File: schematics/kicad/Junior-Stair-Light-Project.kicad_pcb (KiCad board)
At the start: 2 copper layers, 64 x 80 mm, 72 parts, among them J1 12V Eingang, J2 LED_stripes_per_step, T1_1 BC337, T1_10 BC327, T1_11 BC337, T1_12 BC337, T1_13 BC337, T1_14 BC337, T1_15 BC337, T1_16 BC327, T1_17 BC327, T1_18 BC327, T1_19 BC327, T1_2 BC327, T1_20 BC327, T1_21 BC337, T1_22 BC337, T1_23 BC337, T1_24 BC327, T1_25 BC327, T1_26 BC327, T1_3 BC337, T1_4 BC337, T1_5 BC337, T1_6 BC337, T1_7 BC327, T1_8 BC327, T1_9 BC327, U1 L4940V5, U2 Arduino_Nano

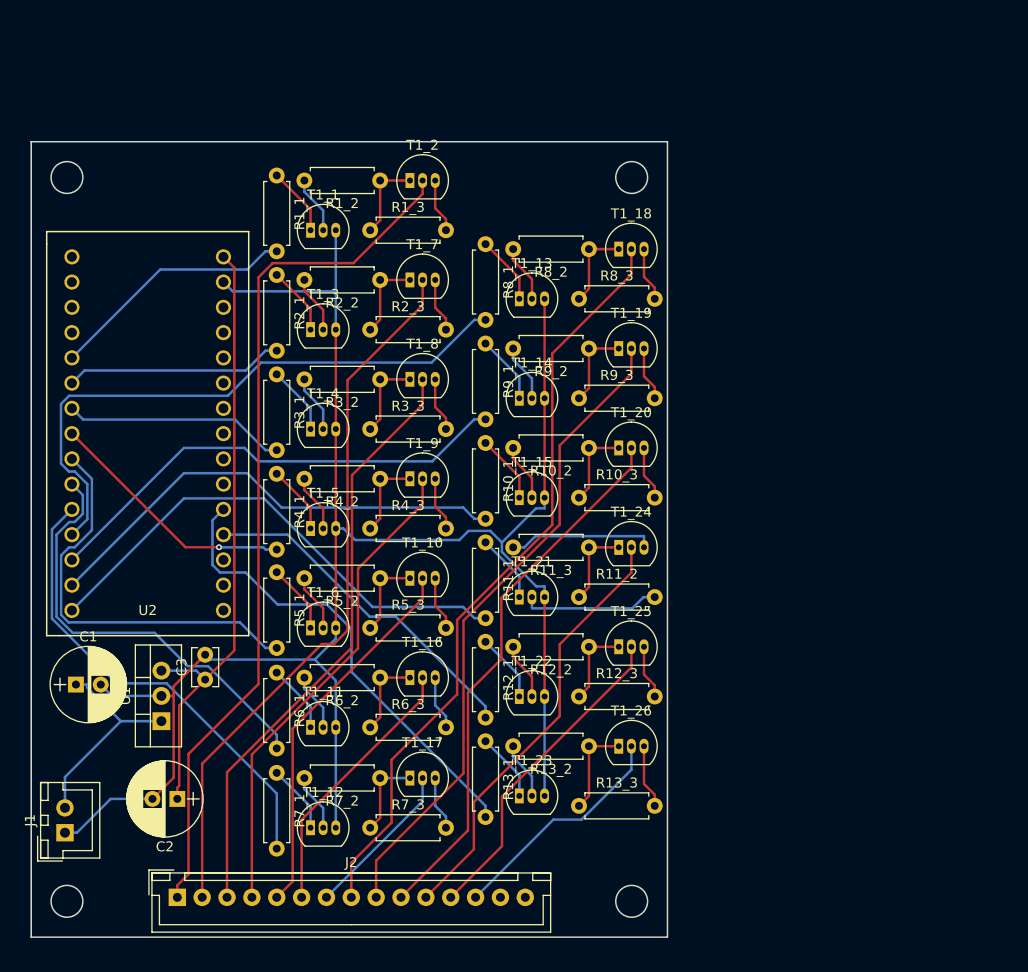
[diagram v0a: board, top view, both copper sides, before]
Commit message: Added max channels (19) and finished first RC of PCB layout
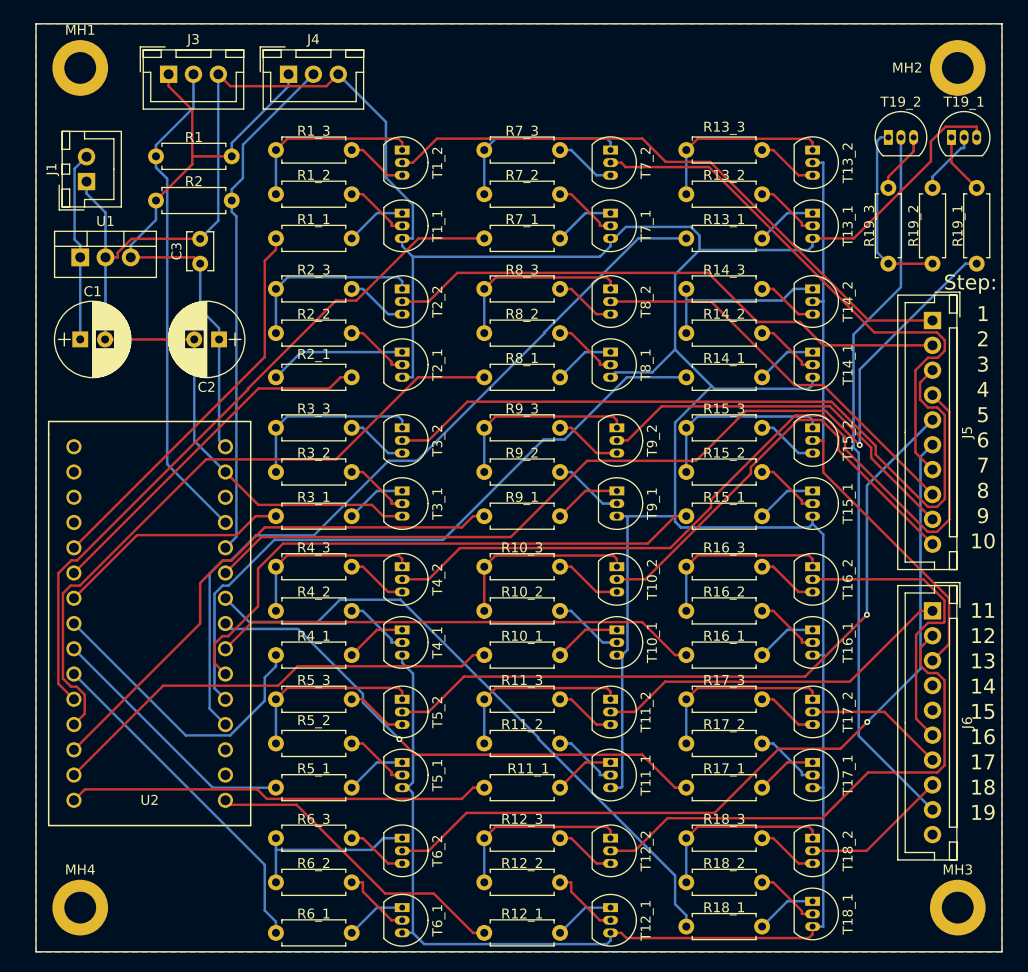
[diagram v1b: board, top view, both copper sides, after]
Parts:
- removed J2: LED_stripes_per_step, Connectors_JST:JST_XH_B15B-XH-A_15x2.50mm_Straight
- removed T1_10, T1_16, T1_17, T1_18, T1_19, T1_20, T1_24, T1_25, T1_26, T1_7, T1_8, T1_9: BC327, TO_SOT_Packages_THT:TO-92_Inline_Narrow_Oval
- removed T1_11, T1_12, T1_13, T1_14, T1_15, T1_21, T1_22, T1_23, T1_3, T1_4, T1_5, T1_6: BC337, TO_SOT_Packages_THT:TO-92_Inline_Narrow_Oval
- added J3: CONN_01X03, Connectors_JST:JST_XH_B03B-XH-A_03x2.50mm_Straight, F.Cu at (123.8, 69.2)
- added J4: CONN_01X03, Connectors_JST:JST_XH_B03B-XH-A_03x2.50mm_Straight, F.Cu at (135.9, 69.2)
- added J5: Conn_01x10, Connectors_JST:JST_XH_B10B-XH-A_10x2.50mm_Straight, F.Cu at (200.7, 94.0)
- added J6: Conn_01x10, Connectors_JST:JST_XH_B10B-XH-A_10x2.50mm_Straight, F.Cu at (200.7, 123.2)
- added MH1: MH1, Mounting_Holes:MountingHole_3.2mm_M3_DIN965_Pad, F.Cu at (114.9, 68.6)
- added MH2: MH2, Mounting_Holes:MountingHole_3.2mm_M3_DIN965_Pad, F.Cu at (203.2, 68.6)
- added MH3: MH3, Mounting_Holes:MountingHole_3.2mm_M3_DIN965_Pad, F.Cu at (203.2, 153.0)
- added MH4: MH4, Mounting_Holes:MountingHole_3.2mm_M3_DIN965_Pad, F.Cu at (114.9, 153.0)
- added R1: 10k, Resistors_THT:R_Axial_DIN0207_L6.3mm_D2.5mm_P7.62mm_Horizontal, F.Cu at (130.2, 77.5)
- added R14_1: 10k, Resistors_THT:R_Axial_DIN0207_L6.3mm_D2.5mm_P7.62mm_Horizontal, F.Cu at (183.5, 99.7)
- added R14_2: 1k, Resistors_THT:R_Axial_DIN0207_L6.3mm_D2.5mm_P7.62mm_Horizontal, F.Cu at (175.9, 95.2)
- added R14_3: 1k, Resistors_THT:R_Axial_DIN0207_L6.3mm_D2.5mm_P7.62mm_Horizontal, F.Cu at (175.9, 90.8)
- added R15_1: 10k, Resistors_THT:R_Axial_DIN0207_L6.3mm_D2.5mm_P7.62mm_Horizontal, F.Cu at (183.5, 113.7)
- added R15_2: 1k, Resistors_THT:R_Axial_DIN0207_L6.3mm_D2.5mm_P7.62mm_Horizontal, F.Cu at (175.9, 109.2)
- added R15_3: 1k, Resistors_THT:R_Axial_DIN0207_L6.3mm_D2.5mm_P7.62mm_Horizontal, F.Cu at (175.9, 104.8)
- added R16_1: 10k, Resistors_THT:R_Axial_DIN0207_L6.3mm_D2.5mm_P7.62mm_Horizontal, F.Cu at (183.5, 127.6)
- added R16_2: 1k, Resistors_THT:R_Axial_DIN0207_L6.3mm_D2.5mm_P7.62mm_Horizontal, F.Cu at (175.9, 123.2)
- added R16_3: 1k, Resistors_THT:R_Axial_DIN0207_L6.3mm_D2.5mm_P7.62mm_Horizontal, F.Cu at (175.9, 118.7)
- added R17_1: 10k, Resistors_THT:R_Axial_DIN0207_L6.3mm_D2.5mm_P7.62mm_Horizontal, F.Cu at (183.5, 141.0)
- added R17_2: 1k, Resistors_THT:R_Axial_DIN0207_L6.3mm_D2.5mm_P7.62mm_Horizontal, F.Cu at (175.9, 136.5)
- added R17_3: 1k, Resistors_THT:R_Axial_DIN0207_L6.3mm_D2.5mm_P7.62mm_Horizontal, F.Cu at (175.9, 132.1)
- added R18_1: 10k, Resistors_THT:R_Axial_DIN0207_L6.3mm_D2.5mm_P7.62mm_Horizontal, F.Cu at (183.5, 154.9)
- added R18_2: 1k, Resistors_THT:R_Axial_DIN0207_L6.3mm_D2.5mm_P7.62mm_Horizontal, F.Cu at (175.9, 150.5)
- added R18_3: 1k, Resistors_THT:R_Axial_DIN0207_L6.3mm_D2.5mm_P7.62mm_Horizontal, F.Cu at (175.9, 146.1)
- added R19_1: 10k, Resistors_THT:R_Axial_DIN0207_L6.3mm_D2.5mm_P7.62mm_Horizontal, F.Cu at (205.1, 80.6)
- added R19_2: 1k, Resistors_THT:R_Axial_DIN0207_L6.3mm_D2.5mm_P7.62mm_Horizontal, F.Cu at (200.7, 88.3)
- added R19_3: 1k, Resistors_THT:R_Axial_DIN0207_L6.3mm_D2.5mm_P7.62mm_Horizontal, F.Cu at (196.2, 88.3)
- added R2: 10k, Resistors_THT:R_Axial_DIN0207_L6.3mm_D2.5mm_P7.62mm_Horizontal, F.Cu at (122.6, 81.9)
- added T10_1: BC337, TO_SOT_Packages_THT:TO-92_Inline_Narrow_Oval, F.Cu at (168.9, 125.1)
- added T10_2: BC327, TO_SOT_Packages_THT:TO-92_Inline_Narrow_Oval, F.Cu at (168.9, 118.7)
- added T11_1: BC337, TO_SOT_Packages_THT:TO-92_Inline_Narrow_Oval, F.Cu at (168.3, 138.4)
- added T11_2: BC327, TO_SOT_Packages_THT:TO-92_Inline_Narrow_Oval, F.Cu at (168.3, 132.1)
- added T12_1: BC337, TO_SOT_Packages_THT:TO-92_Inline_Narrow_Oval, F.Cu at (168.3, 153.0)
- added T12_2: BC327, TO_SOT_Packages_THT:TO-92_Inline_Narrow_Oval, F.Cu at (168.3, 146.1)
- added T13_1: BC337, TO_SOT_Packages_THT:TO-92_Inline_Narrow_Oval, F.Cu at (188.6, 83.2)
- added T13_2: BC327, TO_SOT_Packages_THT:TO-92_Inline_Narrow_Oval, F.Cu at (188.6, 76.8)
- added T14_1: BC337, TO_SOT_Packages_THT:TO-92_Inline_Narrow_Oval, F.Cu at (188.6, 97.2)
- added T14_2: BC327, TO_SOT_Packages_THT:TO-92_Inline_Narrow_Oval, F.Cu at (188.6, 90.8)
- added T15_1: BC337, TO_SOT_Packages_THT:TO-92_Inline_Narrow_Oval, F.Cu at (188.6, 111.1)
- added T15_2: BC327, TO_SOT_Packages_THT:TO-92_Inline_Narrow_Oval, F.Cu at (188.6, 104.8)
- added T16_1: BC337, TO_SOT_Packages_THT:TO-92_Inline_Narrow_Oval, F.Cu at (188.6, 125.1)
- added T16_2: BC327, TO_SOT_Packages_THT:TO-92_Inline_Narrow_Oval, F.Cu at (188.6, 118.7)
- added T17_1: BC337, TO_SOT_Packages_THT:TO-92_Inline_Narrow_Oval, F.Cu at (188.6, 138.4)
- added T17_2: BC327, TO_SOT_Packages_THT:TO-92_Inline_Narrow_Oval, F.Cu at (188.6, 132.1)
- added T18_1: BC337, TO_SOT_Packages_THT:TO-92_Inline_Narrow_Oval, F.Cu at (188.6, 152.4)
- added T18_2: BC327, TO_SOT_Packages_THT:TO-92_Inline_Narrow_Oval, F.Cu at (188.6, 146.1)
- added T19_1: BC337, TO_SOT_Packages_THT:TO-92_Inline_Narrow_Oval, F.Cu at (202.6, 75.6)
- added T19_2: BC327, TO_SOT_Packages_THT:TO-92_Inline_Narrow_Oval, F.Cu at (196.2, 75.6)
- added T2_1: BC337, TO_SOT_Packages_THT:TO-92_Inline_Narrow_Oval, F.Cu at (147.3, 97.2)
- added T2_2: BC327, TO_SOT_Packages_THT:TO-92_Inline_Narrow_Oval, F.Cu at (147.3, 90.8)
- added T3_1: BC337, TO_SOT_Packages_THT:TO-92_Inline_Narrow_Oval, F.Cu at (147.3, 111.1)
- added T3_2: BC327, TO_SOT_Packages_THT:TO-92_Inline_Narrow_Oval, F.Cu at (147.3, 104.8)
- added T4_1: BC337, TO_SOT_Packages_THT:TO-92_Inline_Narrow_Oval, F.Cu at (147.3, 125.1)
- added T4_2: BC327, TO_SOT_Packages_THT:TO-92_Inline_Narrow_Oval, F.Cu at (147.3, 118.7)
- added T5_1: BC337, TO_SOT_Packages_THT:TO-92_Inline_Narrow_Oval, F.Cu at (147.3, 138.4)
- added T5_2: BC327, TO_SOT_Packages_THT:TO-92_Inline_Narrow_Oval, F.Cu at (147.3, 132.1)
- added T6_1: BC337, TO_SOT_Packages_THT:TO-92_Inline_Narrow_Oval, F.Cu at (147.3, 153.0)
- added T6_2: BC327, TO_SOT_Packages_THT:TO-92_Inline_Narrow_Oval, F.Cu at (147.3, 146.1)
- added T7_1: BC337, TO_SOT_Packages_THT:TO-92_Inline_Narrow_Oval, F.Cu at (168.3, 83.2)
- added T7_2: BC327, TO_SOT_Packages_THT:TO-92_Inline_Narrow_Oval, F.Cu at (168.3, 76.8)
- added T8_1: BC337, TO_SOT_Packages_THT:TO-92_Inline_Narrow_Oval, F.Cu at (168.3, 97.2)
- added T8_2: BC327, TO_SOT_Packages_THT:TO-92_Inline_Narrow_Oval, F.Cu at (168.3, 90.8)
- added T9_1: BC337, TO_SOT_Packages_THT:TO-92_Inline_Narrow_Oval, F.Cu at (168.9, 111.1)
- added T9_2: BC327, TO_SOT_Packages_THT:TO-92_Inline_Narrow_Oval, F.Cu at (168.9, 104.8)
- moved R7_3 69.1 mm to (155.6, 76.8)
- moved R13_3 66.8 mm to (175.9, 76.8)
- moved J1 65.5 mm to (115.6, 80.0)
- moved R7_1 60.8 mm to (163.2, 85.7), turned to 180 degrees
- moved R7_2 59.6 mm to (155.6, 81.3), turned to 0 degrees
- moved R13_1 57.7 mm to (183.5, 85.7), turned to 180 degrees
- moved R13_2 56.4 mm to (175.9, 81.3), turned to 0 degrees
- moved U1 47.4 mm to (114.9, 87.6), turned to 0 degrees
- moved C2 46.4 mm to (128.9, 95.9)
- moved C3 41.8 mm to (127.0, 88.3)
- moved C1 34.7 mm to (114.9, 95.9)
- moved R12_1 30.2 mm to (163.2, 155.6), turned to 180 degrees
- moved R6_1 27.2 mm to (142.2, 155.6), turned to 180 degrees
- moved R12_2 25.9 mm to (155.6, 150.5), turned to 0 degrees
- moved R11_1 25.8 mm to (163.2, 141.0), turned to 180 degrees
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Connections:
- U2 pad 16: Net-(U2-Pad16) -> Step12_a
- U2 pad 19: Step12_a -> Step13_a
- U2 pad 20: Step13_a -> Step14_a
- U2 pad 21: Net-(U2-Pad21) -> Step15_a
- U2 pad 22: Net-(U2-Pad22) -> Step16_a
- U2 pad 23: Net-(U2-Pad23) -> Step17_a
- U2 pad 24: Net-(U2-Pad24) -> Step18_a
- U2 pad 25: Net-(U2-Pad25) -> Step19_a
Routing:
- net GND: track 192.1 -> 422.9 mm
- net Step19_a: track 0.00 -> 95.8 mm, vias 0 -> 1
- net Step19: track 0.00 -> 72.9 mm
- net Step14_a: track 0.00 -> 67.5 mm
- net Step18_a: track 0.00 -> 64.3 mm
- net Step15_a: track 0.00 -> 58.5 mm
- net Step6: track 27.1 -> 82.7 mm, vias 0 -> 1
- net Step17_a: track 0.00 -> 53.7 mm, vias 0 -> 1
- net Net-(J4-Pad2): track 0.00 -> 51.7 mm
- net Net-(J3-Pad2): track 0.00 -> 49.5 mm
- net Step16_a: track 0.00 -> 48.8 mm
- net Step7: track 16.0 -> 56.5 mm
- net Step13: track 23.4 -> 60.3 mm
- net Step8: track 76.9 -> 40.4 mm
- net Step5: track 38.2 -> 73.1 mm, vias 0 -> 1
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- added copper zone on B.Cu, net GND
- added copper zone on F.Cu, net GND
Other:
- board size 64 x 80 mm -> 97.2 x 93.3 mm
- board text added: "1"
- board text added: "10"
- board text added: "11"
- board text added: "12"
- board text added: "13"
- board text added: "14"
- board text added: "15"
- board text added: "16"
- board text added: "17"
- board text added: "18"
- board text added: "19"
- board text added: "2"
- board text added: "3"
- board text added: "4"
- board text added: "5"
- board text added: "6"
- board text added: "7"
- board text added: "8"
- board text added: "9"
- board text added: "Step:"
